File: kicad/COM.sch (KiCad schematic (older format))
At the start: 1 part, among them P17 COM

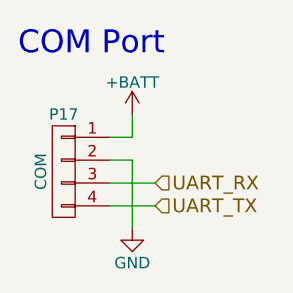
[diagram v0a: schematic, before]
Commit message: 4輪の改良版を設計
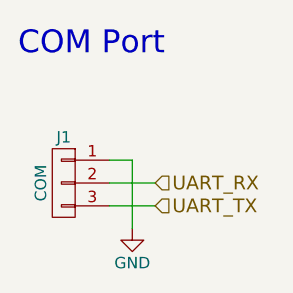
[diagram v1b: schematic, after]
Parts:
- removed P17: COM, Pin_Headers:Pin_Header_Straight_1x04_Pitch1.27mm, symbol CONN_01X04
- added J1: COM, Connectors_JST:JST_SH_BM03B-SRSS-TB_03x1.00mm_Straight, symbol CONN_01X03
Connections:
- net GND: now also J1.1 (P1)
- net UART_RX: now also J1.2 (P2)
- net UART_TX: now also J1.3 (P3)
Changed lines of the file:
@@
 LIBS:zetex
 LIBS:Zilog
-LIBS:KERISE-cache
 EELAYER 25 0
 EELAYER END
 $Descr A4 11693 8268
 encoding utf-8
-Sheet 7 13
+Sheet 7 14
 Title ""
 Date ""
@@
 $EndDescr
 $Comp
-L GND #PWR052
+L GND #PWR053
 U 1 1 57CDAC76
 P 4800 4200
-F 0 "#PWR052" H 4800 3950 50  0001 C CNN
+F 0 "#PWR053" H 4800 3950 50  0001 C CNN
 F 1 "GND" H 4800 4050 50  0000 C CNN
 F 2 "" H 4800 4200 50  0000 C CNN
@@
 COM Port
 $Comp
-L CONN_01X04 P17
-U 1 1 592C4BBD
-P 4500 3950
-F 0 "P17" H 4500 4200 50  0000 C CNN
-F 1 "COM" V 4600 3950 50  0000 C CNN
-F 2 "Pin_Headers:Pin_Header_Straight_1x04_Pitch1.27mm" H 4500 3950 50  0001 C CNN
-F 3 "" H 4500 3950 50  0000 C CNN
-	1    4500 3950
+L CONN_01X03 J1
+U 1 1 59807C31
+P 4500 4000
+F 0 "J1" H 4500 4200 50  0000 C CNN
+F 1 "COM" V 4600 4000 50  0000 C CNN
+F 2 "Connectors_JST:JST_SH_BM03B-SRSS-TB_03x1.00mm_Straight" H 4500 4000 50  0001 C CNN
+F 3 "" H 4500 4000 50  0001 C CNN
+	1    4500 4000
 	-1   0    0    -1
 $EndComp
-$Comp
-L +BATT #PWR053
-U 1 1 592C4BE4
-P 4800 3700
-F 0 "#PWR053" H 4800 3550 50  0001 C CNN
-F 1 "+BATT" H 4800 3840 50  0000 C CNN
-F 2 "" H 4800 3700 50  0000 C CNN
-F 3 "" H 4800 3700 50  0000 C CNN
-	1    4800 3700
-	1    0    0    -1
-$EndComp
-Wire Wire Line
-	4800 3700 4800 3800
-Wire Wire Line
-	4800 3800 4700 3800
 $EndSCHEMATC

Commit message: 実装経験をもとにフットプリントを改良，ミスを修正
SC70サイズのオペアンプのピンアサインを修正
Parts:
- J1: footprint Connectors_JST:JST_SH_BM03B-SRSS-TB_03x1.00mm_Straight -> mouse:JST_SH_BM03B-SRSS-TB_03x1.00mm_Straight
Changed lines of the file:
@@
 $EndDescr
 $Comp
-L GND #PWR059
+L GND #PWR53
 U 1 1 57CDAC76
 P 4800 4200
-F 0 "#PWR059" H 4800 3950 50  0001 C CNN
+F 0 "#PWR53" H 4800 3950 50  0001 C CNN
 F 1 "GND" H 4800 4050 50  0000 C CNN
 F 2 "" H 4800 4200 50  0000 C CNN
@@
 F 0 "J1" H 4500 4200 50  0000 C CNN
 F 1 "COM" V 4600 4000 50  0000 C CNN
-F 2 "Connectors_JST:JST_SH_BM03B-SRSS-TB_03x1.00mm_Straight" H 4500 4000 50  0001 C CNN
+F 2 "mouse:JST_SH_BM03B-SRSS-TB_03x1.00mm_Straight" H 4500 4000 50  0001 C CNN
 F 3 "" H 4500 4000 50  0001 C CNN
 	1    4500 4000
